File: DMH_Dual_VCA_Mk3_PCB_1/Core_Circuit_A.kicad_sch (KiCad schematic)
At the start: 24 parts, among them Q1 BC548, Q2 BC548, U1 TL074

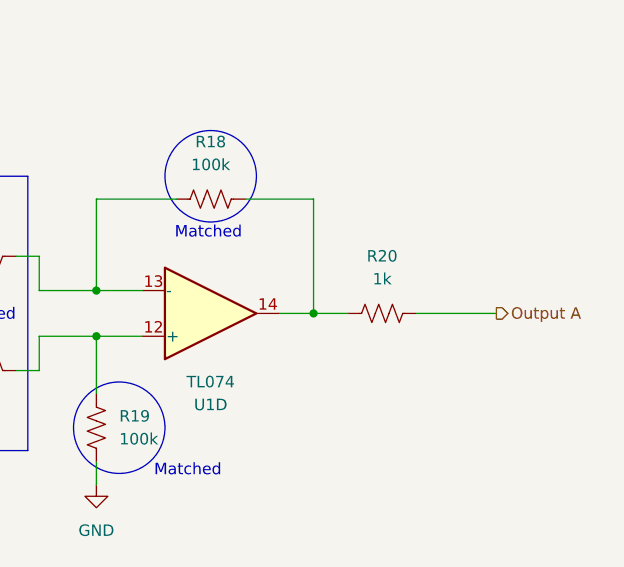
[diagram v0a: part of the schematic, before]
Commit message: 2nd VCA design done
Clipping design in progress
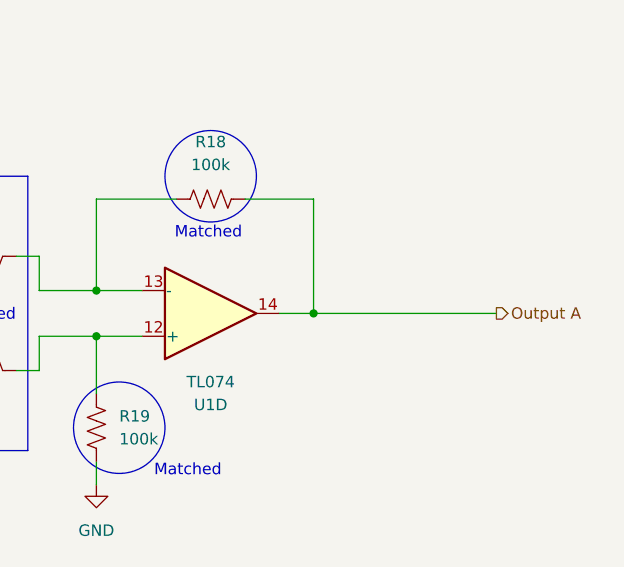
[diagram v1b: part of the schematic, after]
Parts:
- removed R20: 1k, Resistor_THT:R_Axial_DIN0207_L6.3mm_D2.5mm_P7.62mm_Horizontal, symbol Device:R_US
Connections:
- net Output A: now also R18.1, U1.14
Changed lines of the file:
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@@
-	(wire
-		(pts
-			(xy 257.81 50.8) (xy 266.7 50.8)
-		)
-		(stroke
-			(width 0)
-			(type default)
-		)
-	)
 	(wire
 		(pts
@@
 	(wire
 		(pts
-			(xy 246.38 50.8) (xy 250.19 50.8)
+			(xy 246.38 50.8) (xy 266.7 50.8)
 		)
 		(stroke
@@
 		)
 	)
-	(symbol
-		(lib_id "Device:R_US")
-		(at 254 50.8 270)
-		(unit 1)
-		(exclude_from_sim no)
-		(in_bom yes)
-		(on_board yes)
-		(dnp no)
-		(fields_autoplaced yes)
-		(property "Reference" "R20"
-			(at 254 44.45 90)
-			(effects
-				(font
-					(size 1.27 1.27)
-				)
-			)
-		)
-		(property "Value" "1k"
-			(at 254 46.99 90)
-			(effects
-				(font
-					(size 1.27 1.27)
-				)
-			)
-		)
-		(property "Footprint" "Resistor_THT:R_Axial_DIN0207_L6.3mm_D2.5mm_P7.62mm_Horizontal"
-			(at 253.746 51.816 90)
-			(effects
-				(font
-					(size 1.27 1.27)
-				)
-				(hide yes)
-			)
-		)
-		(property "Datasheet" "~"
-			(at 254 50.8 0)
-			(effects
-				(font
-					(size 1.27 1.27)
-				)
-				(hide yes)
-			)
-		)
-		(property "Description" "Resistor, US symbol"
-			(at 254 50.8 0)
-			(effects
-				(font
-					(size 1.27 1.27)
-				)
-				(hide yes)
-			)
-		)
-		(property "Function" ""
-			(at 254 50.8 0)
-			(effects
-				(font
-					(size 1.27 1.27)
-				)
-			)
-		)
-		(pin "1"
-		)
-		(pin "2"
-		)
-		(instances
-			(project "DMH_Transistor_VCA_PCB"
-				(path "/58f4306d-5387-4983-bb08-41a2313fd315/7ad2d702-dfb7-4d49-a82d-34430dd5948f"
-					(reference "R20")
-					(unit 1)
-				)
-			)
-		)
-	)
